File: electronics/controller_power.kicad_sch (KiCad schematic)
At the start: 16 parts, among them U5 TLV75533PDBVR

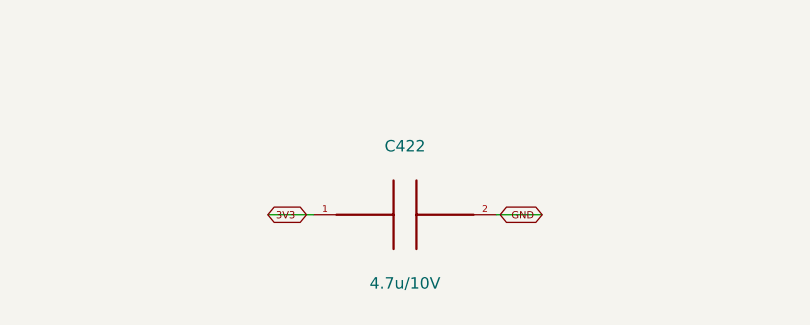
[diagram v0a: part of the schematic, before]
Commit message: Correct audited power BOM and add bounded VM discharge protection
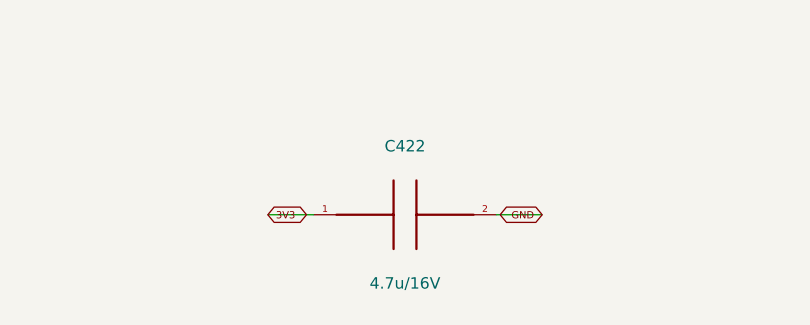
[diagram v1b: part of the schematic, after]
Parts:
- C420, C421: MPN GRM155R61A105KE15D -> GRM155R61C105KA12D
- C422: value 4.7u/10V -> 4.7u/16V; MPN GRM21BR61A475KA73L -> C0805C475K4PACTU; Manufacturer Murata -> KEMET

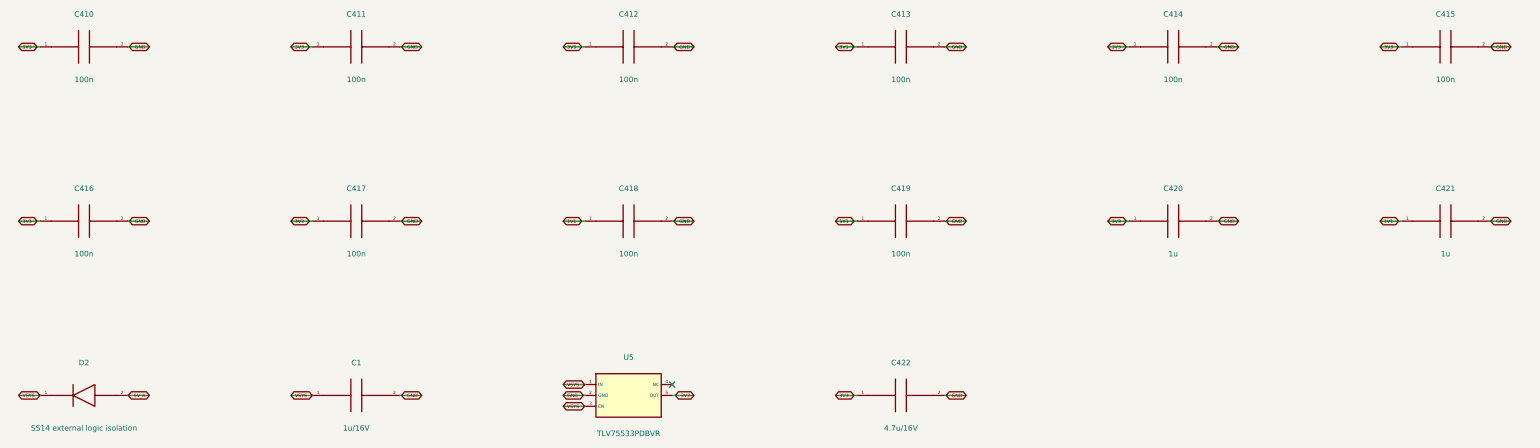
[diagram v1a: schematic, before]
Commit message: Migrate A1 to KiCad 10 and record blocked vendor-model transients
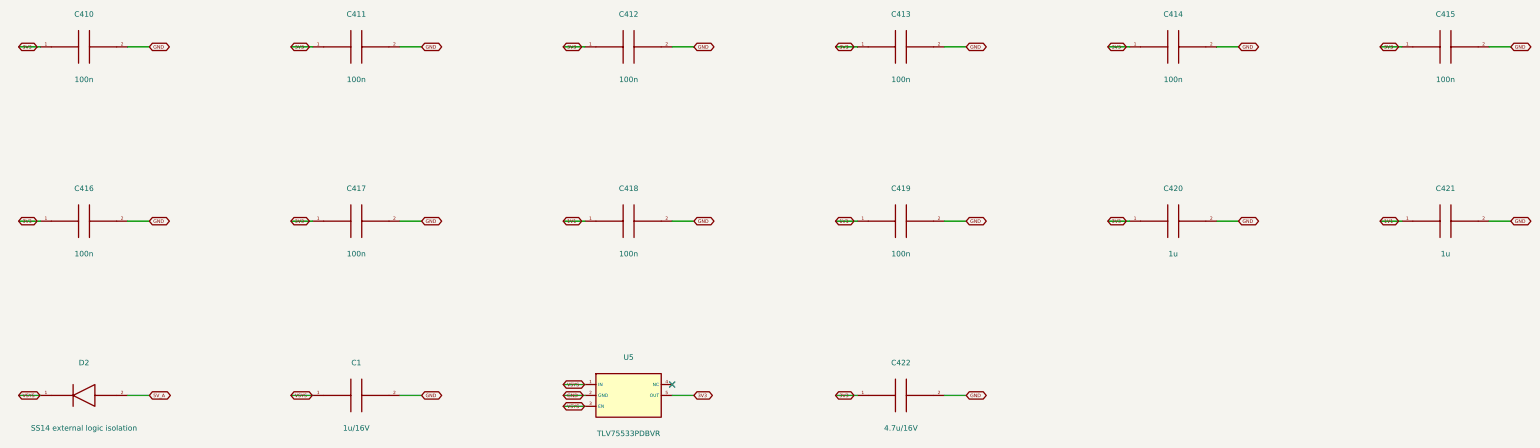
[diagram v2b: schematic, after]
